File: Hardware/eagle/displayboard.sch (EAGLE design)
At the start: 11 parts, among them J1 CON_HEADER_1X08-SMD, J2 FH12-10S-0.5SH, J3 CON_HEADER_1X08-SMD

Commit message: Update to board design
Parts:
- added I2C, UART: CON_HEADER_1X04, dp_devices.v6:CON_HEADER_1X04
- added R1: 100k, rcl:R-EU_R0805
- CN1: device adafruit:JST_2PIN-SMT-RA -> pinhead:PINHD-1X2
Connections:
- removed net N$12: J3.6
- removed net N$13: J3.7
- removed net N$14: J3.8
- removed net N$3: BT1.+, CN1.2
- removed net N$8: J1.8
- new net RX: J3.7, UART.3
- new net SCL: I2C.2, J1.8
- new net SDA: I2C.3, J3.8
- new net TX: J3.6, UART.2
- new net V+: BT1.+, CN1.2, J1.6
- net DISP_EN: now also R1.1
- net GND: now also I2C.4, R1.2, UART.4
- net VCC: now also I2C.1, UART.1
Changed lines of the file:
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@@
 <part name="J3" library="dp_devices.v6" deviceset="CON_HEADER_1X08" device="-SMD"/>
 <part name="P+1" library="supply1" library_urn="urn:adsk.eagle:library:371" deviceset="VCC" device=""/>
-<part name="CN1" library="adafruit" library_urn="urn:adsk.eagle:library:420" deviceset="JST_2PIN" device="-SMT-RA"/>
+<part name="CN1" library="pinhead" library_urn="urn:adsk.eagle:library:325" deviceset="PINHD-1X2" device=""/>
+<part name="P+3" library="supply1" library_urn="urn:adsk.eagle:library:371" deviceset="V+" device=""/>
+<part name="P+4" library="supply1" library_urn="urn:adsk.eagle:library:371" deviceset="V+" device=""/>
+<part name="I2C" library="dp_devices.v6" deviceset="CON_HEADER_1X04" device=""/>
+<part name="P+5" library="supply1" library_urn="urn:adsk.eagle:library:371" deviceset="VCC" device=""/>
+<part name="GND4" library="supply1" library_urn="urn:adsk.eagle:library:371" deviceset="GND" device=""/>
+<part name="UART" library="dp_devices.v6" deviceset="CON_HEADER_1X04" device=""/>
+<part name="P+6" library="supply1" library_urn="urn:adsk.eagle:library:371" deviceset="VCC" device=""/>
+<part name="GND5" library="supply1" library_urn="urn:adsk.eagle:library:371" deviceset="GND" device=""/>
+<part name="R1" library="rcl" library_urn="urn:adsk.eagle:library:334" deviceset="R-EU_" device="R0805" value="100k"/>
 </parts>
 <sheets>
@@
 </instance>
 <instance part="BT1" gate="G$1" x="139.7" y="73.66" rot="R270"/>
-<instance part="GND2" gate="1" x="154.94" y="60.96"/>
+<instance part="GND2" gate="1" x="152.4" y="60.96"/>
 <instance part="U$1" gate="G$1" x="180.34" y="73.66"/>
 <instance part="GND3" gate="1" x="228.6" y="66.04"/>
@@
 </instance>
 <instance part="CN1" gate="G$1" x="121.92" y="76.2" rot="R180"/>
+<instance part="P+3" gate="1" x="218.44" y="144.78" smashed="yes" rot="R90">
+<attribute name="VALUE" x="217.678" y="145.796" size="1.778" layer="96" rot="R180"/>
+</instance>
+<instance part="P+4" gate="1" x="134.62" y="83.82"/>
+<instance part="I2C" gate="J" x="246.38" y="119.38"/>
+<instance part="P+5" gate="VCC" x="241.3" y="127" smashed="yes">
+<attribute name="VALUE" x="243.84" y="129.54" size="1.778" layer="96" rot="R180"/>
+</instance>
+<instance part="GND4" gate="1" x="241.3" y="109.22"/>
+<instance part="UART" gate="J" x="223.52" y="119.38"/>
+<instance part="P+6" gate="VCC" x="215.9" y="127" smashed="yes">
+<attribute name="VALUE" x="218.44" y="129.54" size="1.778" layer="96" rot="R180"/>
+</instance>
+<instance part="GND5" gate="1" x="215.9" y="109.22"/>
+<instance part="R1" gate="G$1" x="160.02" y="66.04" rot="R180"/>
 </instances>
 <busses>
 </busses>
 <nets>
-<net name="N$8" class="0">
+<net name="SCL" class="0">
 <segment>
 <wire x1="233.68" y1="139.7" x2="223.52" y2="139.7" width="0.1524" layer="91"/>
 <pinref part="J1" gate="J" pin="8"/>
+<label x="223.52" y="139.7" size="1.27" layer="95" rot="R180" xref="yes"/>
+</segment>
+<segment>
+<pinref part="I2C" gate="J" pin="2"/>
+<wire x1="246.38" y1="119.38" x2="238.76" y2="119.38" width="0.1524" layer="91"/>
+<label x="238.76" y="119.38" size="1.27" layer="95" rot="R180" xref="yes"/>
 </segment>
 </net>
@@
 <segment>
 <pinref part="U$1" gate="G$1" pin="GND"/>
-<wire x1="167.64" y1="68.58" x2="154.94" y2="68.58" width="0.1524" layer="91"/>
+<wire x1="167.64" y1="68.58" x2="152.4" y2="68.58" width="0.1524" layer="91"/>
 <pinref part="GND2" gate="1" pin="GND"/>
-<wire x1="154.94" y1="68.58" x2="151.384" y2="68.58" width="0.1524" layer="91"/>
-<wire x1="154.94" y1="68.58" x2="154.94" y2="63.5" width="0.1524" layer="91"/>
-<junction x="154.94" y="68.58"/>
+<wire x1="152.4" y1="68.58" x2="151.384" y2="68.58" width="0.1524" layer="91"/>
+<wire x1="152.4" y1="68.58" x2="152.4" y2="66.04" width="0.1524" layer="91"/>
+<junction x="152.4" y="68.58"/>
 <pinref part="C3" gate="G$1" pin="-"/>
+<wire x1="152.4" y1="66.04" x2="152.4" y2="63.5" width="0.1524" layer="91"/>
 <wire x1="151.384" y1="69.85" x2="151.384" y2="68.58" width="0.1524" layer="91"/>
+<pinref part="R1" gate="G$1" pin="2"/>
+<wire x1="154.94" y1="66.04" x2="152.4" y2="66.04" width="0.1524" layer="91"/>
+<junction x="152.4" y="66.04"/>
 </segment>
 <segment>
@@
 <wire x1="220.98" y1="69.596" x2="220.98" y2="68.58" width="0.1524" layer="91"/>
 </segment>
+<segment>
+<pinref part="I2C" gate="J" pin="4"/>
+<pinref part="GND4" gate="1" pin="GND"/>
+<wire x1="246.38" y1="114.3" x2="241.3" y2="114.3" width="0.1524" layer="91"/>
+<wire x1="241.3" y1="114.3" x2="241.3" y2="111.76" width="0.1524" layer="91"/>
+</segment>
+<segment>
+<pinref part="UART" gate="J" pin="4"/>
+<pinref part="GND5" gate="1" pin="GND"/>
+<wire x1="223.52" y1="114.3" x2="215.9" y2="114.3" width="0.1524" layer="91"/>
+<wire x1="215.9" y1="114.3" x2="215.9" y2="111.76" width="0.1524" layer="91"/>
+</segment>
 </net>
 <net name="VCC" class="0">
@@
 <junction x="160.02" y="78.74"/>
 </segment>
+<segment>
+<pinref part="I2C" gate="J" pin="1"/>
+<pinref part="P+5" gate="VCC" pin="VCC"/>
+<wire x1="246.38" y1="121.92" x2="241.3" y2="121.92" width="0.1524" layer="91"/>
+<wire x1="241.3" y1="121.92" x2="241.3" y2="124.46" width="0.1524" layer="91"/>
+</segment>
+<segment>
+<pinref part="UART" gate="J" pin="1"/>
+<pinref part="P+6" gate="VCC" pin="VCC"/>
+<wire x1="223.52" y1="121.92" x2="215.9" y2="121.92" width="0.1524" layer="91"/>
+<wire x1="215.9" y1="121.92" x2="215.9" y2="124.46" width="0.1524" layer="91"/>
+</segment>
 </net>
 <net name="N$1" class="0">
@@
 </segment>
 </net>
-<net name="N$12" class="0">
+<net name="TX" class="0">
 <segment>
 <wire x1="243.84" y1="144.78" x2="256.54" y2="144.78" width="0.1524" layer="91"/>
 <pinref part="J3" gate="J" pin="6"/>
-</segment>
-</net>
-<net name="N$13" class="0">
+<label x="256.54" y="144.78" size="1.27" layer="95" xref="yes"/>
+</segment>
+<segment>
+<pinref part="UART" gate="J" pin="2"/>
+<wire x1="223.52" y1="119.38" x2="215.9" y2="119.38" width="0.1524" layer="91"/>
+<label x="215.9" y="119.38" size="1.27" layer="95" rot="R180" xref="yes"/>
+</segment>
+</net>
+<net name="RX" class="0">
 <segment>
 <wire x1="243.84" y1="142.24" x2="256.54" y2="142.24" width="0.1524" layer="91"/>
 <pinref part="J3" gate="J" pin="7"/>
-</segment>
-</net>
-<net name="N$14" class="0">
+<label x="256.54" y="142.24" size="1.27" layer="95" xref="yes"/>
+</segment>
+<segment>
+<pinref part="UART" gate="J" pin="3"/>
+<wire x1="223.52" y1="116.84" x2="215.9" y2="116.84" width="0.1524" layer="91"/>
+<label x="215.9" y="116.84" size="1.27" layer="95" rot="R180" xref="yes"/>
+</segment>
+</net>
+<net name="SDA" class="0">
 <segment>
 <wire x1="243.84" y1="139.7" x2="256.54" y2="139.7" width="0.1524" layer="91"/>
 <pinref part="J3" gate="J" pin="8"/>
+<label x="256.54" y="139.7" size="1.27" layer="95" xref="yes"/>
+</segment>
+<segment>
+<pinref part="I2C" gate="J" pin="3"/>
+<wire x1="246.38" y1="116.84" x2="238.76" y2="116.84" width="0.1524" layer="91"/>
+<label x="238.76" y="116.84" size="1.27" layer="95" rot="R180" xref="yes"/>
 </segment>
 </net>
@@
 <wire x1="167.64" y1="73.66" x2="165.1" y2="73.66" width="0.1524" layer="91"/>
 <label x="165.1" y="73.66" size="1.27" layer="95" rot="R180" xref="yes"/>
+<pinref part="R1" gate="G$1" pin="1"/>
+<wire x1="165.1" y1="66.04" x2="165.1" y2="73.66" width="0.1524" layer="91"/>
 </segment>
 <segment>
@@
 </segment>
 </net>
-<net name="N$3" class="0">
-<segment>
-<pinref part="BT1" gate="G$1" pin="+"/>
-<wire x1="129.54" y1="78.74" x2="139.7" y2="78.74" width="0.1524" layer="91"/>
-<wire x1="129.54" y1="78.74" x2="129.54" y2="76.2" width="0.1524" layer="91"/>
-<pinref part="CN1" gate="G$1" pin="2"/>
-<wire x1="129.54" y1="76.2" x2="124.46" y2="76.2" width="0.1524" layer="91"/>
-</segment>
-</net>
 <net name="N$5" class="0">
 <segment>
@@
 </segment>
 </net>
+<net name="V+" class="0">
+<segment>
+<pinref part="BT1" gate="G$1" pin="+"/>
+<wire x1="129.54" y1="78.74" x2="134.62" y2="78.74" width="0.1524" layer="91"/>
+<wire x1="134.62" y1="78.74" x2="139.7" y2="78.74" width="0.1524" layer="91"/>
+<wire x1="129.54" y1="78.74" x2="129.54" y2="76.2" width="0.1524" layer="91"/>
+<pinref part="CN1" gate="G$1" pin="2"/>
+<wire x1="129.54" y1="76.2" x2="124.46" y2="76.2" width="0.1524" layer="91"/>
+<pinref part="P+4" gate="1" pin="V+"/>
+<wire x1="134.62" y1="81.28" x2="134.62" y2="78.74" width="0.1524" layer="91"/>
+<junction x="134.62" y="78.74"/>
+</segment>
+<segment>
+<pinref part="J1" gate="J" pin="6"/>
+<wire x1="233.68" y1="144.78" x2="220.98" y2="144.78" width="0.1524" layer="91"/>
+<pinref part="P+3" gate="1" pin="V+"/>
+</segment>
+</net>

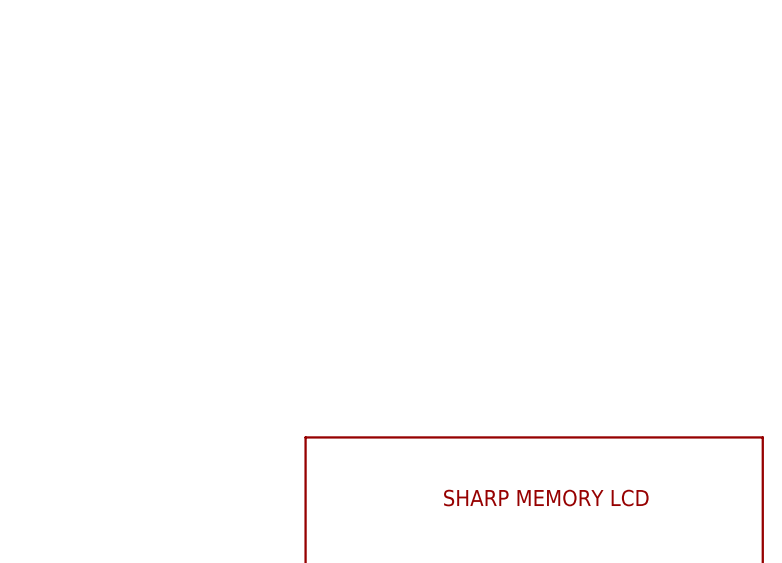
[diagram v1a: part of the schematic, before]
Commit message: Fixup board routing & add EEPROM for identity storage
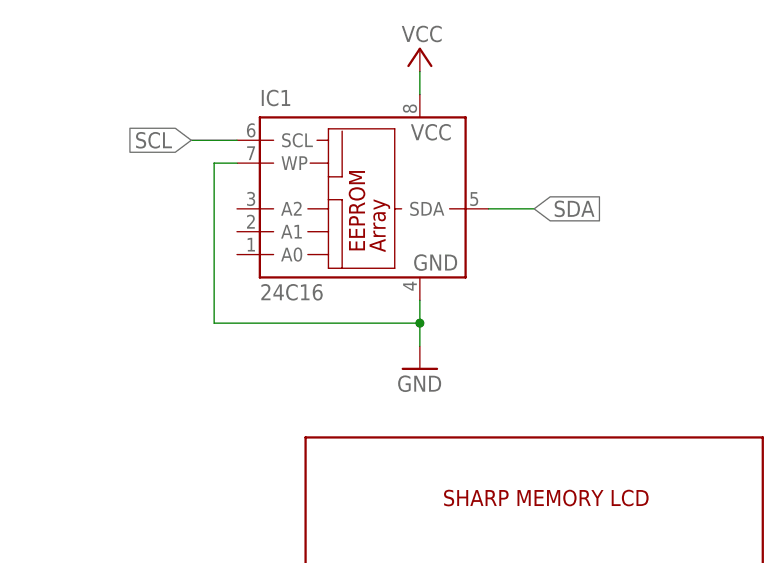
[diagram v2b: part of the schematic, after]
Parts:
- added IC1: 24C16, microchip:24C04SN
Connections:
- net GND: now also IC1.GND, IC1.WP
- net SCL: now also IC1.SCL
- net SDA: now also IC1.SDA
- net VCC: now also IC1.VCC
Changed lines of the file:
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@@
 <part name="GND5" library="supply1" library_urn="urn:adsk.eagle:library:371" deviceset="GND" device=""/>
 <part name="R1" library="rcl" library_urn="urn:adsk.eagle:library:334" deviceset="R-EU_" device="R0805" value="100k"/>
+<part name="IC1" library="microchip" library_urn="urn:adsk.eagle:library:294" deviceset="24C*" device="SN" technology="04" value="24C16"/>
+<part name="GND6" library="supply1" library_urn="urn:adsk.eagle:library:371" deviceset="GND" device=""/>
+<part name="P+7" library="supply1" library_urn="urn:adsk.eagle:library:371" deviceset="VCC" device=""/>
 </parts>
 <sheets>
@@
 <instance part="GND5" gate="1" x="215.9" y="109.22"/>
 <instance part="R1" gate="G$1" x="160.02" y="66.04" rot="R180"/>
+<instance part="IC1" gate="G$1" x="157.48" y="154.94"/>
+<instance part="GND6" gate="1" x="165.1" y="137.16"/>
+<instance part="P+7" gate="VCC" x="165.1" y="172.72" smashed="yes">
+<attribute name="VALUE" x="167.64" y="175.26" size="1.778" layer="96" rot="R180"/>
+</instance>
 </instances>
 <busses>
@@
 <wire x1="246.38" y1="119.38" x2="238.76" y2="119.38" width="0.1524" layer="91"/>
 <label x="238.76" y="119.38" size="1.27" layer="95" rot="R180" xref="yes"/>
+</segment>
+<segment>
+<pinref part="IC1" gate="G$1" pin="SCL"/>
+<wire x1="144.78" y1="162.56" x2="139.7" y2="162.56" width="0.1524" layer="91"/>
+<label x="139.7" y="162.56" size="1.778" layer="95" rot="R180" xref="yes"/>
 </segment>
 </net>
@@
 <wire x1="215.9" y1="114.3" x2="215.9" y2="111.76" width="0.1524" layer="91"/>
 </segment>
+<segment>
+<pinref part="IC1" gate="G$1" pin="WP"/>
+<wire x1="144.78" y1="160.02" x2="142.24" y2="160.02" width="0.1524" layer="91"/>
+<wire x1="142.24" y1="160.02" x2="142.24" y2="142.24" width="0.1524" layer="91"/>
+<wire x1="142.24" y1="142.24" x2="165.1" y2="142.24" width="0.1524" layer="91"/>
+<pinref part="IC1" gate="G$1" pin="GND"/>
+<wire x1="165.1" y1="144.78" x2="165.1" y2="142.24" width="0.1524" layer="91"/>
+<pinref part="GND6" gate="1" pin="GND"/>
+<wire x1="165.1" y1="142.24" x2="165.1" y2="139.7" width="0.1524" layer="91"/>
+<junction x="165.1" y="142.24"/>
+</segment>
 </net>
 <net name="VCC" class="0">
@@
 <wire x1="215.9" y1="121.92" x2="215.9" y2="124.46" width="0.1524" layer="91"/>
 </segment>
+<segment>
+<pinref part="IC1" gate="G$1" pin="VCC"/>
+<pinref part="P+7" gate="VCC" pin="VCC"/>
+<wire x1="165.1" y1="167.64" x2="165.1" y2="170.18" width="0.1524" layer="91"/>
+</segment>
 </net>
 <net name="N$1" class="0">
@@
 <label x="238.76" y="116.84" size="1.27" layer="95" rot="R180" xref="yes"/>
 </segment>
-</net>
+<segment>
+<pinref part="IC1" gate="G$1" pin="SDA"/>
+<wire x1="172.72" y1="154.94" x2="177.8" y2="154.94" width="0.1524" layer="91"/>
+<label x="177.8" y="154.94" size="1.778" layer="95" xref="yes"/>
+</segment>
+</net>
